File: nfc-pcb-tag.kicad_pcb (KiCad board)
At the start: 2 copper layers, 16 parts, among them IC1 NT3H2111W0FHKH, J1 Conn_ARM_SWD_TagConnect_TC203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, U1 CH32V003FxUx

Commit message: Tweak firmware
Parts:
- removed C3, C4, C5: C, Capacitor_SMD:C_0402_1005Metric
- removed D2: LED, LED_SMD:LED_0402_1005Metric
- removed R6: 1k, Resistor_SMD:R_0402_1005Metric
- added C6: C, Capacitor_SMD:C_0402_1005Metric, B.Cu at (69.8, 39.2)
- added C7: C, Capacitor_SMD:C_0402_1005Metric, B.Cu at (69.8, 40.2)
- moved C2 30.3 mm to (69.8, 38.2)
- moved R2 21.8 mm to (80.8, 38.5)
- moved R1 21.7 mm to (80.8, 37.5)
- moved D1 16.4 mm to (72.5, 47.0), turned to 0 degrees
- moved R5 15.1 mm to (72.5, 47.0)
- moved R3 9.22 mm to (75.2, 32.2), turned to 0 degrees
- moved R4 9.22 mm to (69.8, 32.2)
- moved U1 7.54 mm to (80.0, 34.0), turned to -135 degrees
- moved IC1 0.75 mm to (72.5, 40.0)
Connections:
- C1 pad 1: Net-(IC1-LB) -> Net-(IC1-LA)
- IC1 pad 8: Net-(IC1-LB) -> Net-(IC1-LA)
- J1 pad 3: /RST -> unconnected-(J1-~{RESET}-Pad3)
- U1 pad 1: /RST -> unconnected-(U1-PD7-Pad1)
- U1 pad 12: unconnected-(U1-PC5-Pad12) -> GND
- U1 pad 19: /A0 -> /A1
- U1 pad 20: /A1 -> /A0
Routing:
- net +3.3V: track 0.00 -> 34.1 mm, vias 0 -> 2
- net GND: track 1.93 -> 27.2 mm, vias 0 -> 4
- net /LED0: track 0.00 -> 24.8 mm, vias 0 -> 2
- net /SWDIO: track 0.00 -> 15.4 mm
- net /SDA: track 0.00 -> 15.1 mm, vias 0 -> 2
- net Net-(IC1-LA): track 0.00 -> 12.3 mm, vias 0 -> 2
- net /SCL: track 0.00 -> 11.2 mm
- net /A1: track 0.00 -> 10.4 mm
- net /A0: track 0.00 -> 4.47 mm
- net Net-(R4-Pad1): track 0.00 -> 1.97 mm
- net Net-(D1-A): track 0.00 -> 1.91 mm, vias 0 -> 1
- net Net-(R3-Pad1): track 0.00 -> 1.80 mm
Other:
- board outline added: 22.1 x 19.5 mm
- board text added: "Willow"

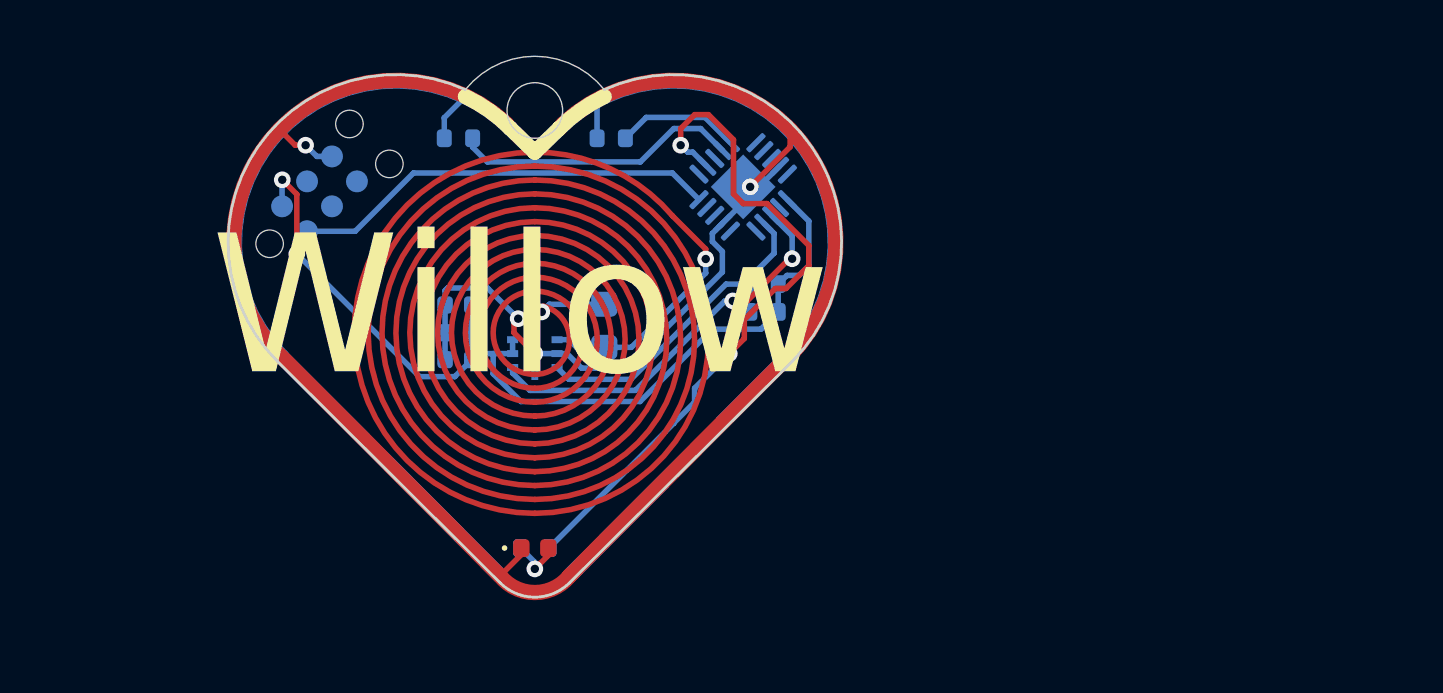
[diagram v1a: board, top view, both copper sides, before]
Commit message: Convert to inductor antenna
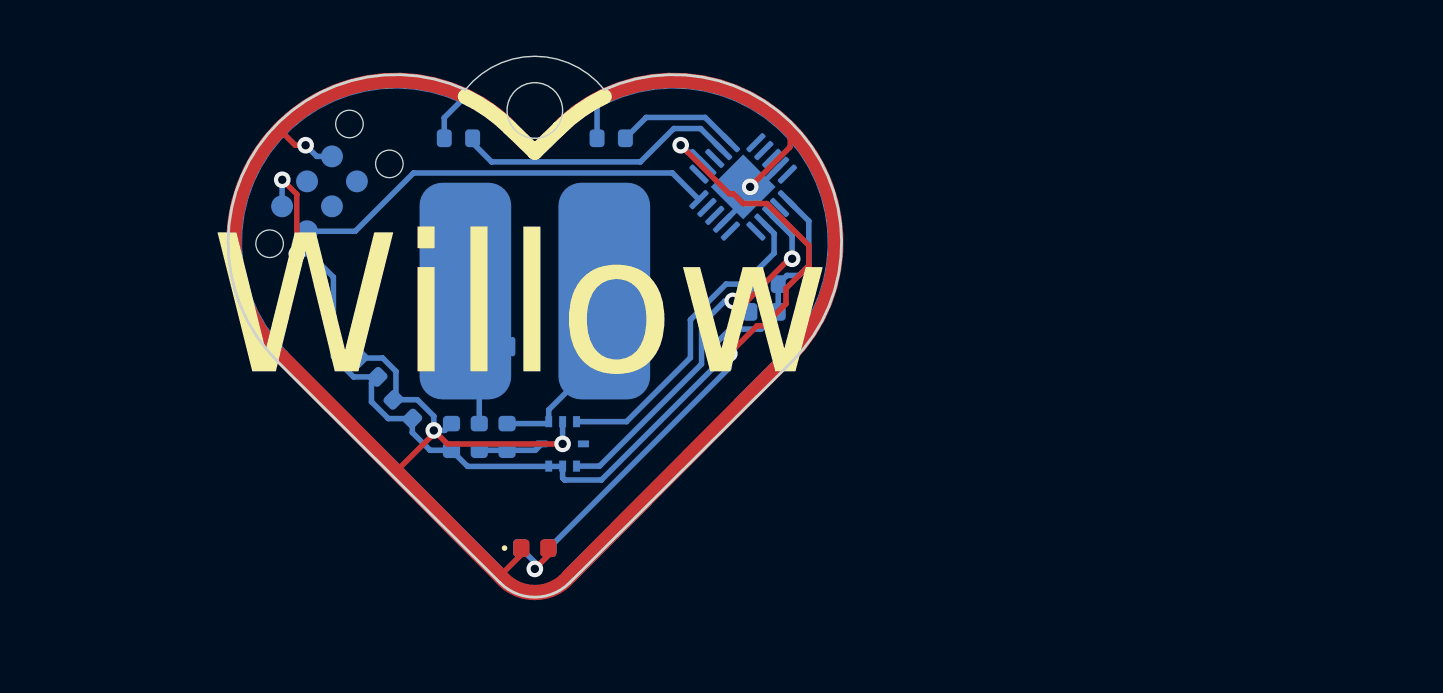
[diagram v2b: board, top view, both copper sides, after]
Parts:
- added C3: C, Capacitor_SMD:C_0402_1005Metric, B.Cu at (70.5, 43.0)
- added TP3: TestPoint_2Pole, Library:ANT, B.Cu at (72.5, 37.8)
- C1: footprint Capacitor_SMD:C_0603_1608Metric -> Capacitor_SMD:C_0402_1005Metric
- moved C1 5.32 mm to (71.5, 43.0), turned to 90 degrees
- moved C2 3.95 mm to (66.5, 40.5), turned to 135 degrees
- moved C6 3.40 mm to (67.8, 42.0), turned to 135 degrees
- moved IC1 3.40 mm to (73.5, 43.2), turned to -90 degrees
- moved C7 2.79 mm to (69.5, 43.0), turned to 90 degrees
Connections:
- C1 pad 1: Net-(IC1-LA) -> Net-(IC1-LB)
- IC1 pad 8: Net-(IC1-LA) -> Net-(IC1-LB)
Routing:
- net Net-(C3-Pad1): track 0.00 -> 5.48 mm
- net Net-(IC1-LA): track 12.3 -> 7.06 mm, vias 2 -> 0
- net /LED0: track 24.8 -> 22.3 mm
- net Net-(IC1-LB): track 0.00 -> 2.35 mm
- net +3.3V: track 34.1 -> 35.6 mm
- net GND: track 27.2 -> 28.1 mm
- net /SDA: track 15.1 -> 14.3 mm
- net /SCL: track 11.2 -> 11.8 mm

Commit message: Run kiibot
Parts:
- C2, C6: value C -> 10uF
- C3: value C -> 68p
- C7: value C -> 100nF
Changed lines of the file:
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@@
 		)
 	)
+	(property "GIT_TAG" "V0.1")
+	(property "PROJ_TITLE" "nfc-pcb-tag")
 	(net 0 "")
 	(net 1 "Net-(IC1-LA)")
@@
 			)
 		)
+		(property "LCSC Part" "C5336761 "
+			(at 0 0 0)
+			(unlocked yes)
+			(layer "F.Fab")
+			(hide yes)
+			(effects
+				(font
+					(size 1 1)
+					(thickness 0.15)
+				)
+			)
+		)
 		(property ki_fp_filters "LED* LED_SMD:* LED_THT:*")
 		(sheetname "Root")
@@
 			)
 		)
+		(property "LCSC Part" "C60490"
+			(at 0 0 0)
+			(unlocked yes)
+			(layer "B.Fab")
+			(hide yes)
+			(effects
+				(font
+					(size 1 1)
+					(thickness 0.15)
+				)
+				(justify mirror)
+			)
+		)
 		(property ki_fp_filters "R_*")
 		(sheetname "Root")
@@
 			)
 		)
+		(property "LCSC Part" "C60490"
+			(at 0 0 180)
+			(unlocked yes)
+			(layer "B.Fab")
+			(hide yes)
+			(effects
+				(font
+					(size 1 1)
+					(thickness 0.15)
+				)
+				(justify mirror)
+			)
+		)
 		(property ki_fp_filters "R_*")
 		(sheetname "Root")
@@
 			)
 		)
+		(property "LCSC Part" "C60490"
+			(at 0 0 180)
+			(unlocked yes)
+			(layer "B.Fab")
+			(hide yes)
+			(effects
+				(font
+					(size 1 1)
+					(thickness 0.15)
+				)
+				(justify mirror)
+			)
+		)
 		(property ki_fp_filters "R_*")
 		(sheetname "Root")
@@
 			)
 		)
+		(property "LCSC Part" "C60490"
+			(at 0 0 0)
+			(unlocked yes)
+			(layer "B.Fab")
+			(hide yes)
+			(effects
+				(font
+					(size 1 1)
+					(thickness 0.15)
+				)
+				(justify mirror)
+			)
+		)
 		(property ki_fp_filters "R_*")
 		(sheetname "Root")
@@
 			)
 		)
+		(property "LCSC Part" "C5299908"
+			(at 0 0 -135)
+			(unlocked yes)
+			(layer "B.Fab")
+			(hide yes)
+			(effects
+				(font
+					(size 1 1)
+					(thickness 0.15)
+				)
+				(justify mirror)
+			)
+		)
 		(property ki_fp_filters "QFN*1EP*3x3mm*P0.4mm*EP1.65x1.65mm*")
 		(sheetname "Root")
@@
 			)
 		)
-		(property "Value" "C"
+		(property "Value" "10uF"
 			(at 0 -1.16 -45)
 			(layer "B.Fab")
@@
 			)
 		)
+		(property "LCSC Part" "C15525"
+			(at 0 0 135)
+			(unlocked yes)
+			(layer "B.Fab")
+			(hide yes)
+			(effects
+				(font
+					(size 1 1)
+					(thickness 0.15)
+				)
+				(justify mirror)
+			)
+		)
 		(property ki_fp_filters "C_*")
 		(sheetname "Root")
@@
 			)
 		)
-		(property "Value" "C"
+		(property "Value" "10uF"
 			(at 0 -1.16 -45)
 			(layer "B.Fab")
@@
 			)
 		)
+		(property "LCSC Part" "C15525"
+			(at 0 0 135)
+			(unlocked yes)
+			(layer "B.Fab")
+			(hide yes)
+			(effects
+				(font
+					(size 1 1)
+					(thickness 0.15)
+				)
+				(justify mirror)
+			)
+		)
 		(property ki_fp_filters "C_*")
 		(sheetname "Root")
@@
 			)
 		)
+		(property "LCSC Part" "C114759 "
+			(at 0 0 180)
+			(unlocked yes)
+			(layer "B.Fab")
+			(hide yes)
+			(effects
+				(font
+					(size 1 1)
+					(thickness 0.15)
+				)
+				(justify mirror)
+			)
+		)
 		(property ki_fp_filters "R_*")
 		(sheetname "Root")
@@
 			)
 		)
-		(property "Value" "C"
+		(property "Value" "68p"
 			(at 0 -1.43 90)
 			(layer "B.Fab")
@@
 			)
 		)
+		(property "LCSC Part" "C107010"
+			(at 0 0 -90)
+			(unlocked yes)
+			(layer "B.Fab")
+			(hide yes)
+			(effects
+				(font
+					(size 1 1)
+					(thickness 0.15)
+				)
+				(justify mirror)
+			)
+		)
 		(property ki_fp_filters "C_*")
 		(sheetname "Root")
@@
 			)
 		)
-		(property "Value" "C"
+		(property "Value" "100nF"
 			(at 0 -1.16 90)
 			(layer "B.Fab")
@@
 			)
 		)
+		(property "LCSC Part" "C541406"
+			(at 0 0 90)
+			(unlocked yes)
+			(layer "B.Fab")
+			(hide yes)
+			(effects
+				(font
+					(size 1 1)
+					(thickness 0.15)
+				)
+				(justify mirror)
+			)
+		)
 		(property ki_fp_filters "C_*")
 		(sheetname "Root")
@@
 			(unlocked yes)
 			(layer "B.Fab")
+			(hide yes)
+			(effects
+				(font
+					(size 1 1)
+					(thickness 0.15)
+				)
+				(justify mirror)
+			)
+		)
+		(property "LCSC Part" "C33126958"
+			(at 0 0 180)
+			(unlocked yes)
+			(layer "B.Fab")

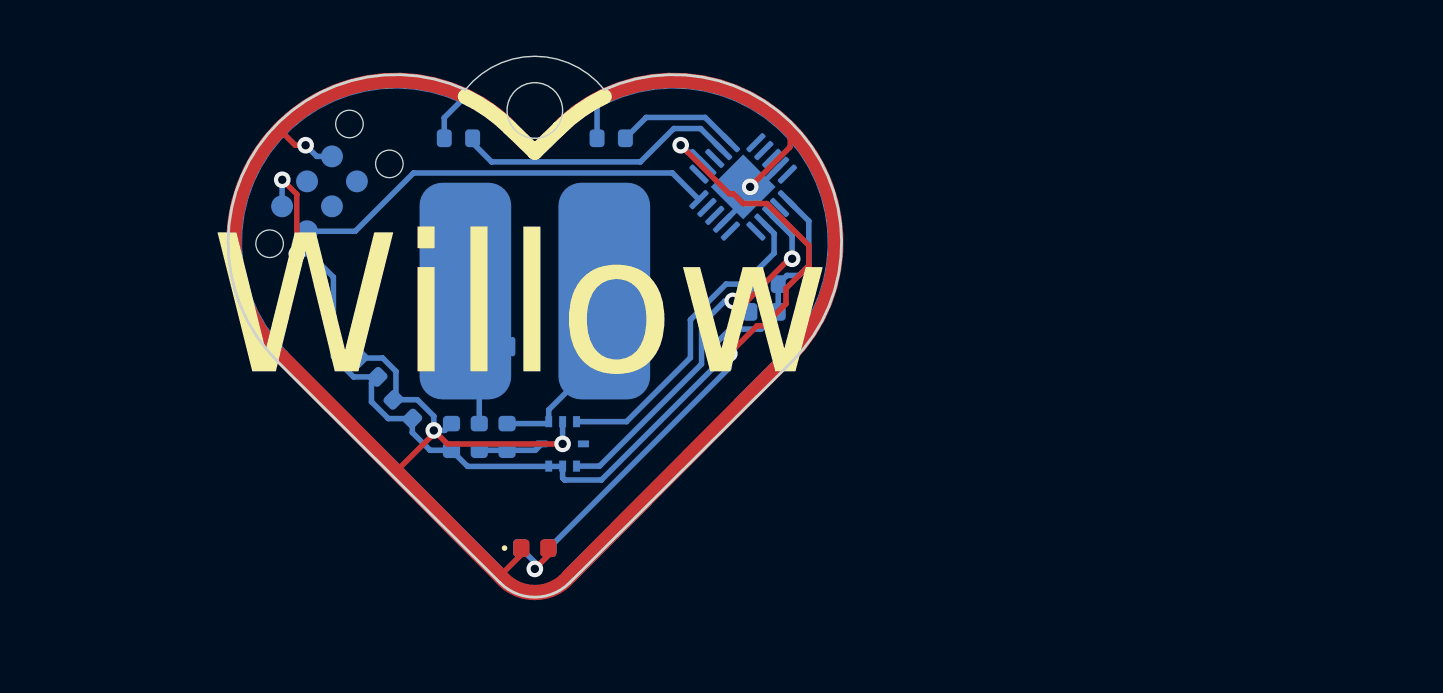
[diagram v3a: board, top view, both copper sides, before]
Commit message: Revise to use buttons
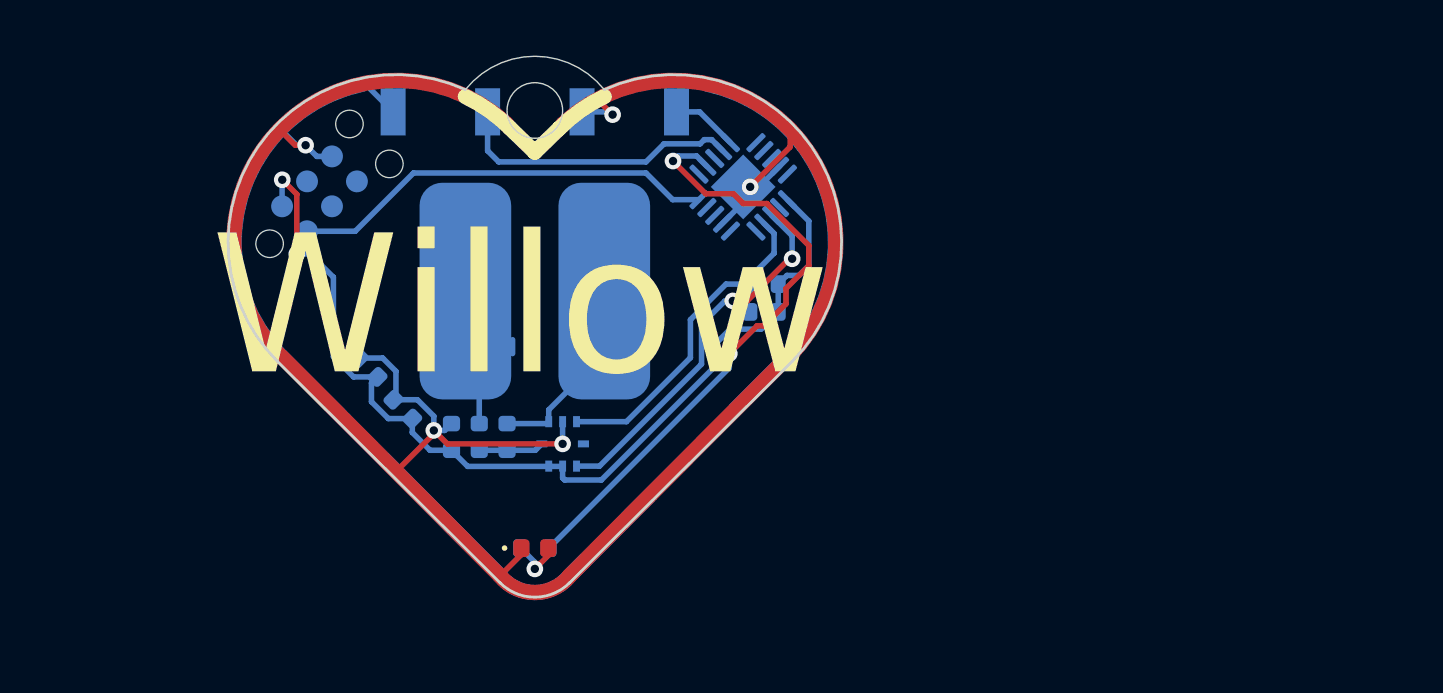
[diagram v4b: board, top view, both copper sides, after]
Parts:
- removed R3, R4: 10k, Resistor_SMD:R_0402_1005Metric
- added SW1: SW_Push, Button_Switch_SMD:SW_SPST_B3U-3000P, B.Cu at (75.9, 31.3)
- added SW2: SW_Push, Button_Switch_SMD:SW_SPST_B3U-3000P, B.Cu at (69.1, 31.3)
- ANT1: renamed from TP3; value TestPoint_2Pole -> ANT
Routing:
- net GND: track 28.1 -> 32.7 mm, vias 4 -> 5
- net /A0: track 4.47 -> 2.40 mm
- net Net-(R4-Pad1): track 1.97 -> 0.00 mm
- net Net-(R3-Pad1): track 1.80 -> 0.00 mm
